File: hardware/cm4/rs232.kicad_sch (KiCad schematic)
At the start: 13 parts, among them J3 D340 PC-Schnittstelle, U3 ADuM5211, U5 MAX3232E

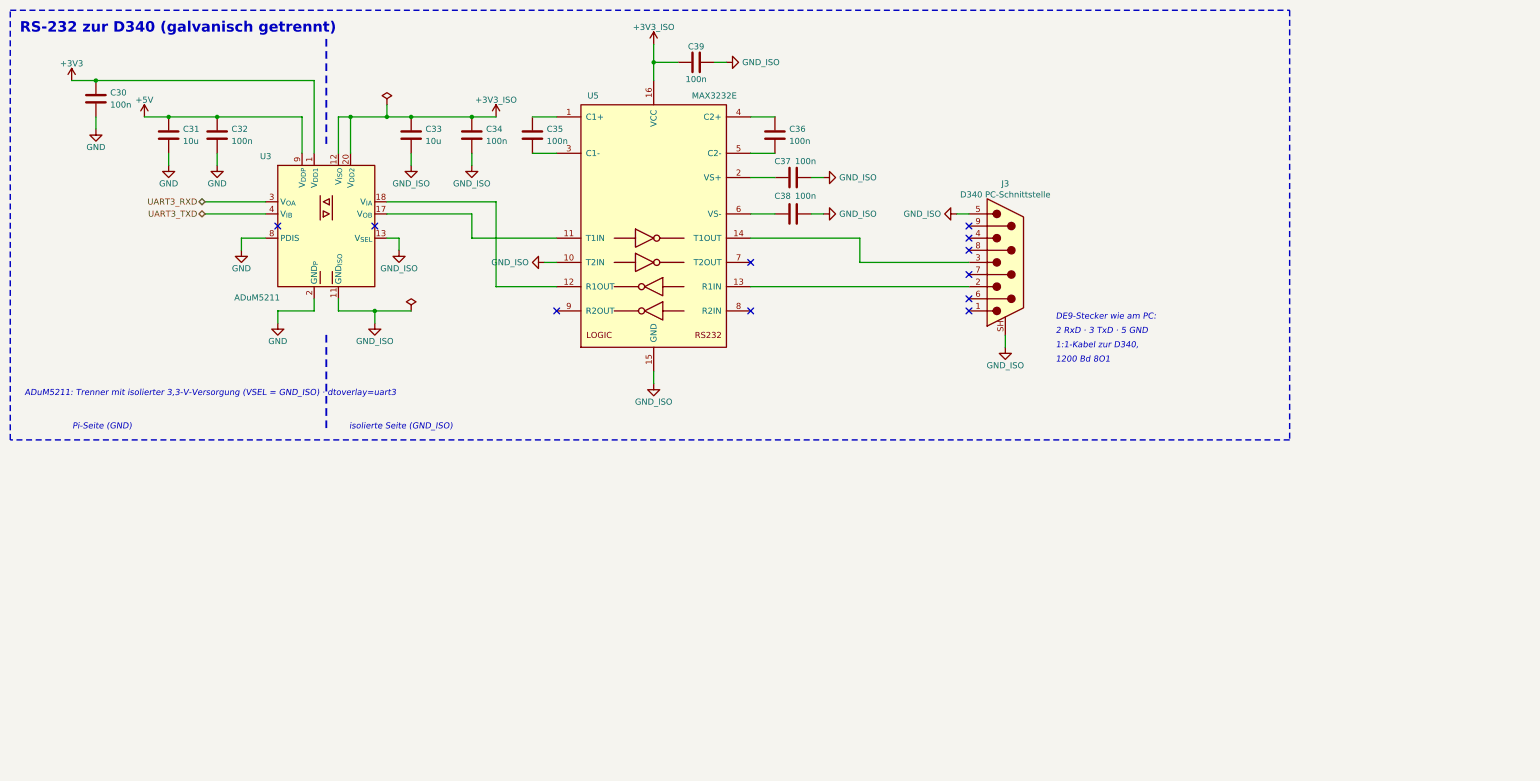
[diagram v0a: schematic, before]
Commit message: CM4-Schaltplan: Einzelblock-Blätter ohne Rahmen, Inhalt zentriert
kicadgen: Steht nur ein Block auf einem Blatt, entfällt der Rahmen (sein Titel wird
Blatttitel) und der Inhalt wird auf dem Blatt zentriert (über dem Schriftfeld, auf dem
1,27-mm-Raster). Hinweistexte der CM4-Blätter an die Schaltungen gerückt.

Co-Authored-By: Claude Opus 5.5 <noreply@anthropic.com>
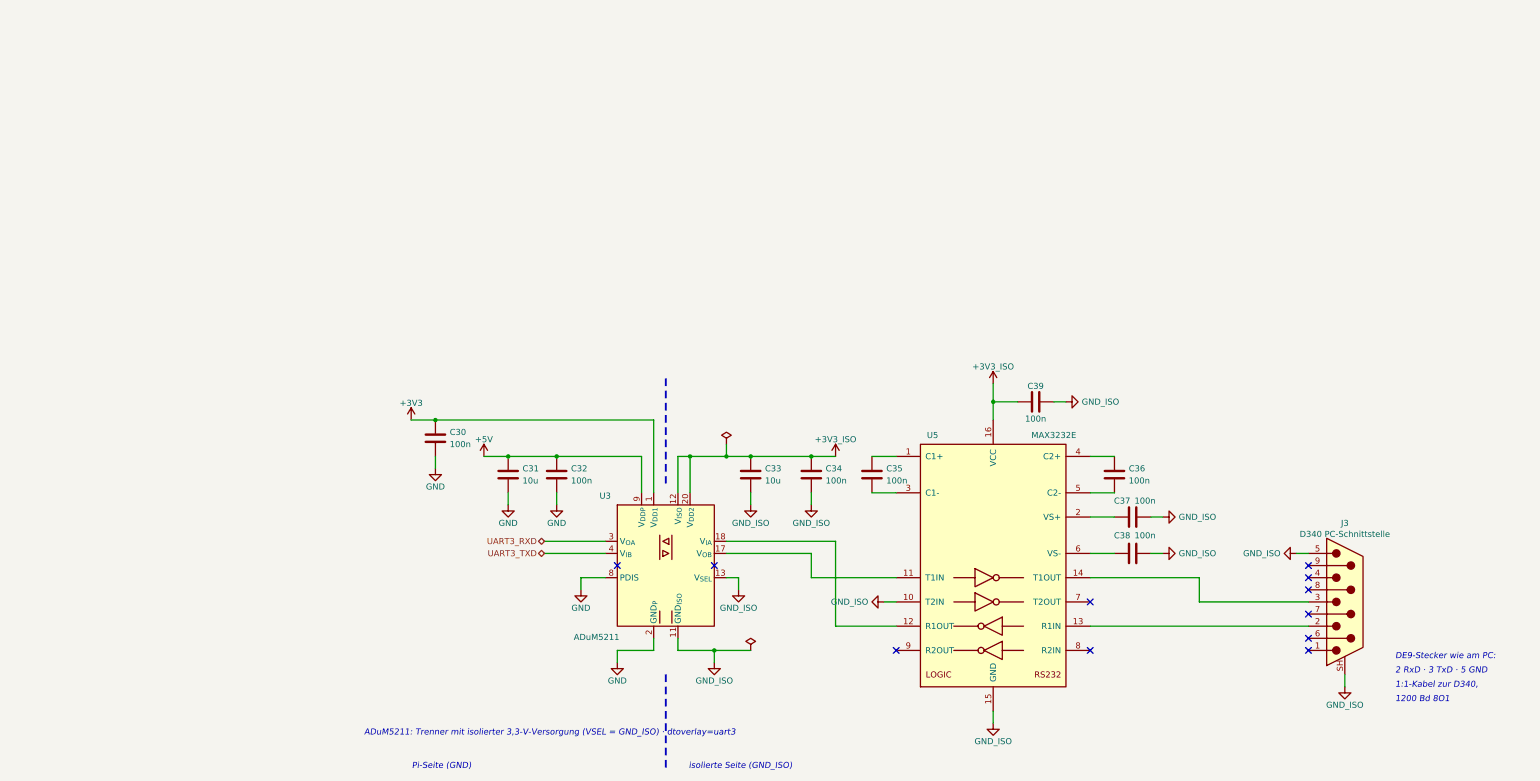
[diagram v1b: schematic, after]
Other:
- note removed: "RS-232 zur D340 (galvanisch getrennt)"
- title: RS-232 -> RS-232 zur D340 (galvanisch getrennt)
